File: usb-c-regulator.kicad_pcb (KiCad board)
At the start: 2 copper layers, 19 x 23 mm, 8 parts, among them J1 Conn_01x02, J2 USB_C_Receptacle_PowerOnly_6P, U1 ADM7172ACPZ-3.3-R7

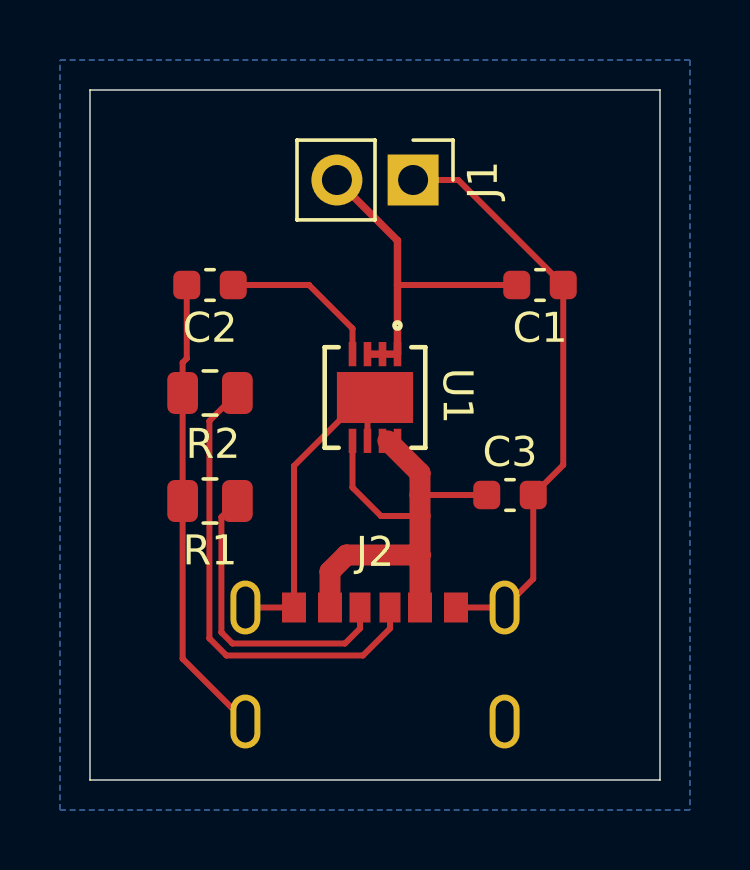
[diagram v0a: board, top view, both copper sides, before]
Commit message: adjusted clearance of pad 9 on ADM7172 footprint
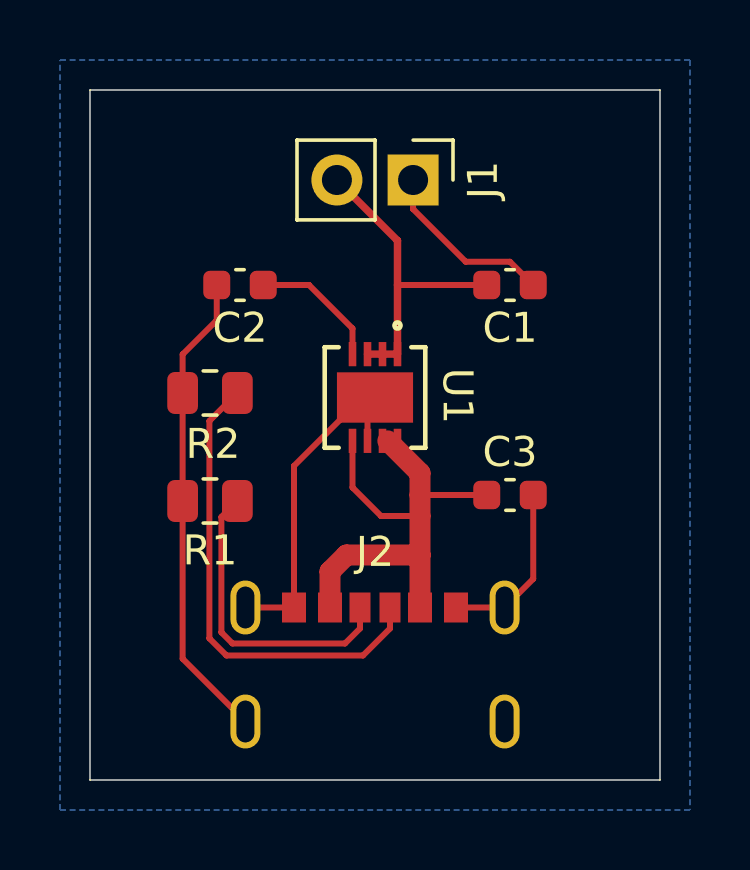
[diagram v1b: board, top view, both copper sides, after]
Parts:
- moved C1 1.00 mm to (116.0, 106.5)
- moved C2 1.00 mm to (107.0, 106.5)
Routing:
- net GND: track 46.6 -> 38.4 mm
- net Net-(U1-SS): track 5.43 -> 4.43 mm
- net +3.3V: track 11.6 -> 10.6 mm
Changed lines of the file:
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@@
 		(tags "resistor")
 		(property "Reference" "R1"
-			(at 0 -1.65 360)
+			(at 0 -1.65 0)
 			(layer "F.SilkS")
 			(effects
@@
 		)
 		(fp_text user "${REFERENCE}"
-			(at 0 0 360)
+			(at 0 0 0)
 			(layer "F.Fab")
 			(effects
@@
 				(font
 					(size 1 1)
-					(thickness 0.1)
+					(thickness 0.15)
 				)
 			)
@@
 	(footprint "Capacitor_SMD:C_0603_1608Metric"
 		(layer "F.Cu")
-		(at 106 106.5 180)
+		(at 107 106.5 180)
 		(descr "Capacitor SMD 0603 (1608 Metric), square (rectangular) end terminal, IPC_7351 nominal, (Body size source: IPC-SM-782 page 76, https://www.pcb-3d.com/wordpress/wp-content/uploads/ipc-sm-782a_amendment_1_and_2.pdf), generated with kicad-footprint-generator")
 		(tags "capacitor")
 		(property "Reference" "C2"
-			(at 0 -1.43 360)
+			(at 0 -1.43 0)
 			(layer "F.SilkS")
 			(effects
@@
 		)
 		(property "Value" "1nF"
-			(at 0 1.43 360)
+			(at 0 1.43 0)
 			(layer "F.Fab")
 			(effects
@@
 		)
 		(fp_text user "${REFERENCE}"
-			(at 0 0 360)
+			(at 0 0 0)
 			(layer "F.Fab")
 			(effects
@@
 		(pad "9" smd rect
 			(at 0 0 270)
-			(size 1.7018 2.54)
+			(size 1.68 2.54)
 			(layers "F.Cu" "F.Paste" "F.Mask")
 			(net 2 "GND")
@@
 		(tags "resistor")
 		(property "Reference" "R2"
-			(at -0.1 -1.7 360)
+			(at -0.1 -1.7 0)
 			(layer "F.SilkS")
 			(effects
@@
 		)
 		(fp_text user "${REFERENCE}"
-			(at 0 0 360)
+			(at 0 0 0)
 			(layer "F.Fab")
 			(effects
@@
 	(footprint "Capacitor_SMD:C_0603_1608Metric"
 		(layer "F.Cu")
-		(at 117 106.5 180)
+		(at 116 106.5 180)
 		(descr "Capacitor SMD 0603 (1608 Metric), square (rectangular) end terminal, IPC_7351 nominal, (Body size source: IPC-SM-782 page 76, https://www.pcb-3d.com/wordpress/wp-content/uploads/ipc-sm-782a_amendment_1_and_2.pdf), generated with kicad-footprint-generator")
 		(tags "capacitor")
 		(property "Reference" "C1"
-			(at 0 -1.43 360)
+			(at 0 -1.43 0)
 			(layer "F.SilkS")
 			(effects
@@
 		)
 		(property "Value" "4.7uF"
-			(at 0 1.43 360)
+			(at 0 1.43 0)
 			(layer "F.Fab")
 			(effects
@@
 		)
 		(fp_text user "${REFERENCE}"
-			(at 0 0 360)
+			(at 0 0 0)
 			(layer "F.Fab")
 			(effects
@@
 	)
 	(segment
+		(start 115.225 106.5)
+		(end 112.250001 106.5)
+		(width 0.2)
+		(layer "F.Cu")
+		(net 1)
+	)
+	(segment
 		(start 112.250001 106.5)
 		(end 112.250001 108.804601)
@@
 	)
 	(segment
-		(start 116.225 106.5)
-		(end 112.250001 106.5)
-		(width 0.2)
-		(layer "F.Cu")
-		(net 1)
-	)
-	(segment
 		(start 112.250001 105.020001)
 		(end 112.250001 106.5)
@@
 	)
 	(segment
-		(start 117.775 112.5)
-		(end 116.775 113.5)
+		(start 116 105.725)
+		(end 114.525 105.725)
+		(width 0.2)
+		(layer "F.Cu")
+		(net 2)
+	)
+	(segment
+		(start 112.77 103.97)
+		(end 112.77 103)
 		(width 0.2)
 		(layer "F.Cu")
@@
 	)
 	(segment
-		(start 105.0875 109.0875)
-		(end 105.225 108.95)
-		(width 0.2)
-		(layer "F.Cu")
-		(net 2)
-	)
-	(segment
-		(start 105.0875 110.1)
-		(end 105.0875 109.0875)
-		(width 0.2)
-		(layer "F.Cu")
-		(net 2)
-	)
-	(segment
-		(start 111.25 110.500001)
-		(end 111.5 110.250001)
+		(start 106.225 106.5)
+		(end 106.225 107.675)
 		(width 0.2)
 		(layer "F.Cu")
@@
 	)
 	(segment
-		(start 105.225 108.95)
-		(end 105.225 106.5)
-		(width 0.2)
-		(layer "F.Cu")
-		(net 2)
-	)
-	(segment
-		(start 117.775 106.5)
-		(end 117.775 112.5)
+		(start 105.0875 108.8125)
+		(end 105.0875 110.1)
 		(width 0.2)
 		(layer "F.Cu")
@@
 	)
 	(segment
+		(start 116.775 106.5)
+		(end 116 105.725)
+		(width 0.2)
+		(layer "F.Cu")
+		(net 2)
+	)
+	(segment
 		(start 108.8 117.25)
 		(end 107.18 117.25)
@@
 	)
 	(segment
-		(start 114.275 103)
-		(end 112.77 103)
+		(start 114.525 105.725)
+		(end 112.77 103.97)
+		(width 0.2)
+		(layer "F.Cu")
+		(net 2)
+	)
+	(segment
+		(start 106.225 107.675)
+		(end 105.0875 108.8125)
 		(width 0.2)
 		(layer "F.Cu")
@@
 	)
 	(segment
-		(start 117.775 106.5)
-		(end 114.275 103)
-		(width 0.2)
-		(layer "F.Cu")
-		(net 2)
-	)
-	(segment
-		(start 111.5 110.250001)
-		(end 111.0809 110.250001)
-		(width 0.2)
-		(layer "F.Cu")
-		(net 2)
-	)
-	(segment
 		(start 108.8 112.530901)
 		(end 108.8 117.25)
@@
 	)
 	(segment
-		(start 106.775 106.5)
+		(start 107.775 106.5)
 		(end 109.3 106.5)
 		(width 0.2)
